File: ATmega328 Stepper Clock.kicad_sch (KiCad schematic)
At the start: 14 parts, among them IC1 ATMEGA328-AU, J2 SBH11-PBPC-D05-ST-BK, M1 Stepper_Motor_bipolar, M2 Stepper_Motor_bipolar, Q1 TCRT5000, Q2 TCRT5000, Y1 Crystal

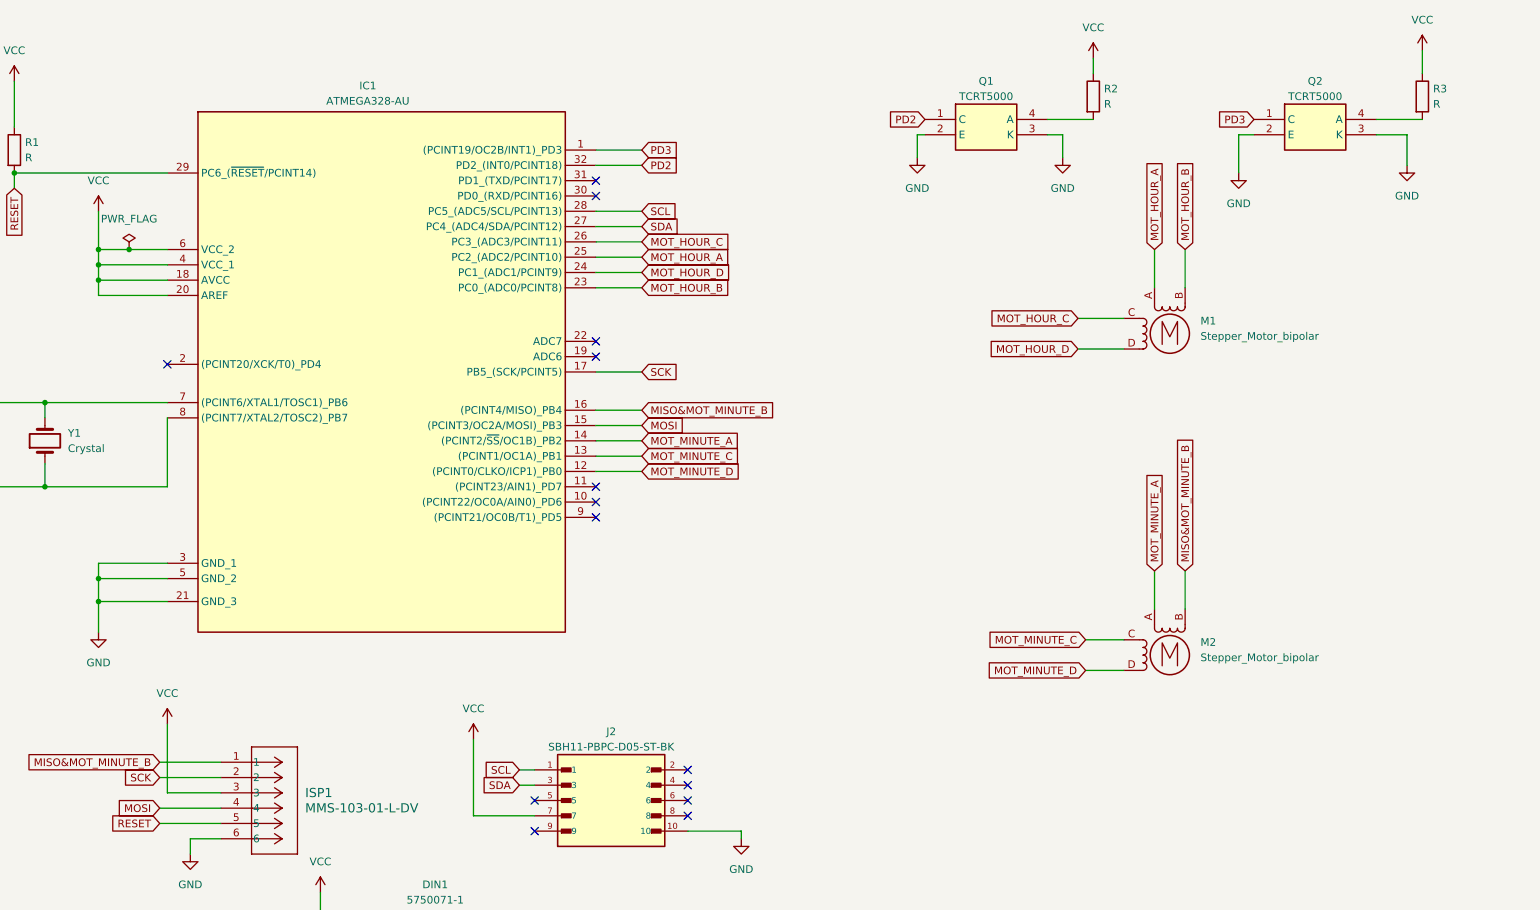
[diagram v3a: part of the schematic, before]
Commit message: I have made custom symbol for VID28-05 and assigned the footprint for it which sir gave me
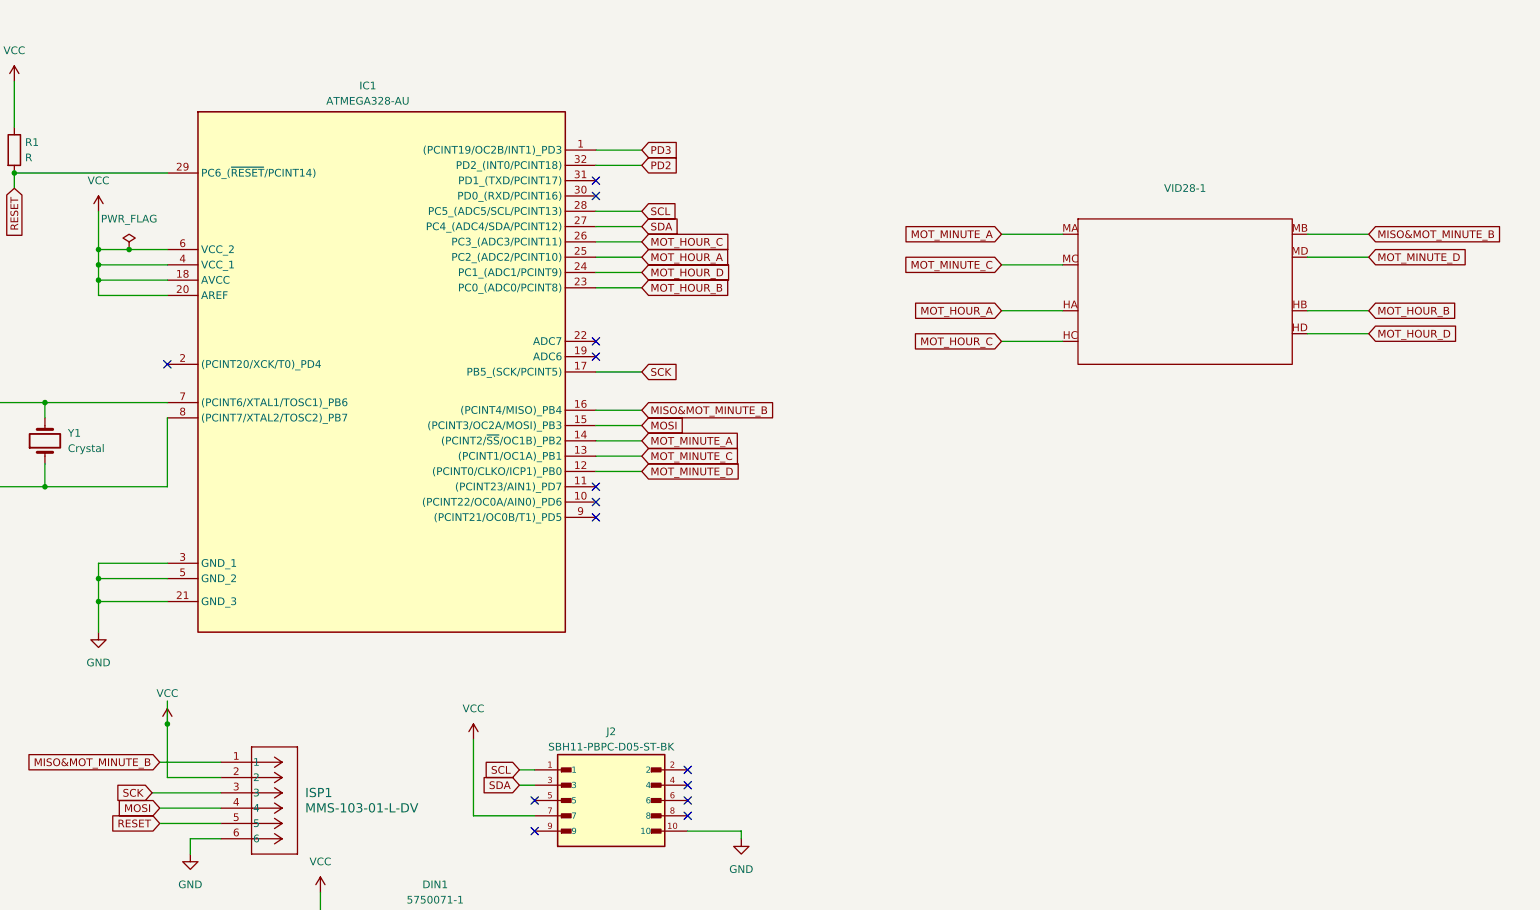
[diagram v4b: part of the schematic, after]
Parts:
- removed M1, M2: Stepper_Motor_bipolar, symbol Motor:Stepper_Motor_bipolar
- removed Q1, Q2: TCRT5000, SamacSys_Parts:TCRT5000, symbol SamacSys_Parts:TCRT5000
- removed R2, R3: R, Resistor_THT:R_Axial_DIN0414_L11.9mm_D4.5mm_P15.24mm_Horizontal, symbol Device:R
- added VID28-1: ~, VID28-05:VID28-05, symbol VID28-05:VID28-05
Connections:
- net MISO&MOT_MINUTE_B: now also VID28-1.MB
- net MOT_HOUR_A: now also VID28-1.HA
- net MOT_HOUR_B: now also VID28-1.HB
- net MOT_HOUR_C: now also VID28-1.HC
- net MOT_HOUR_D: now also VID28-1.HD
- net MOT_MINUTE_A: now also VID28-1.MA
- net MOT_MINUTE_C: now also VID28-1.MC
- net MOT_MINUTE_D: now also VID28-1.MD
- net SCK: now also ISP1.3; no longer ISP1.2
- net VCC: now also ISP1.2; no longer ISP1.3

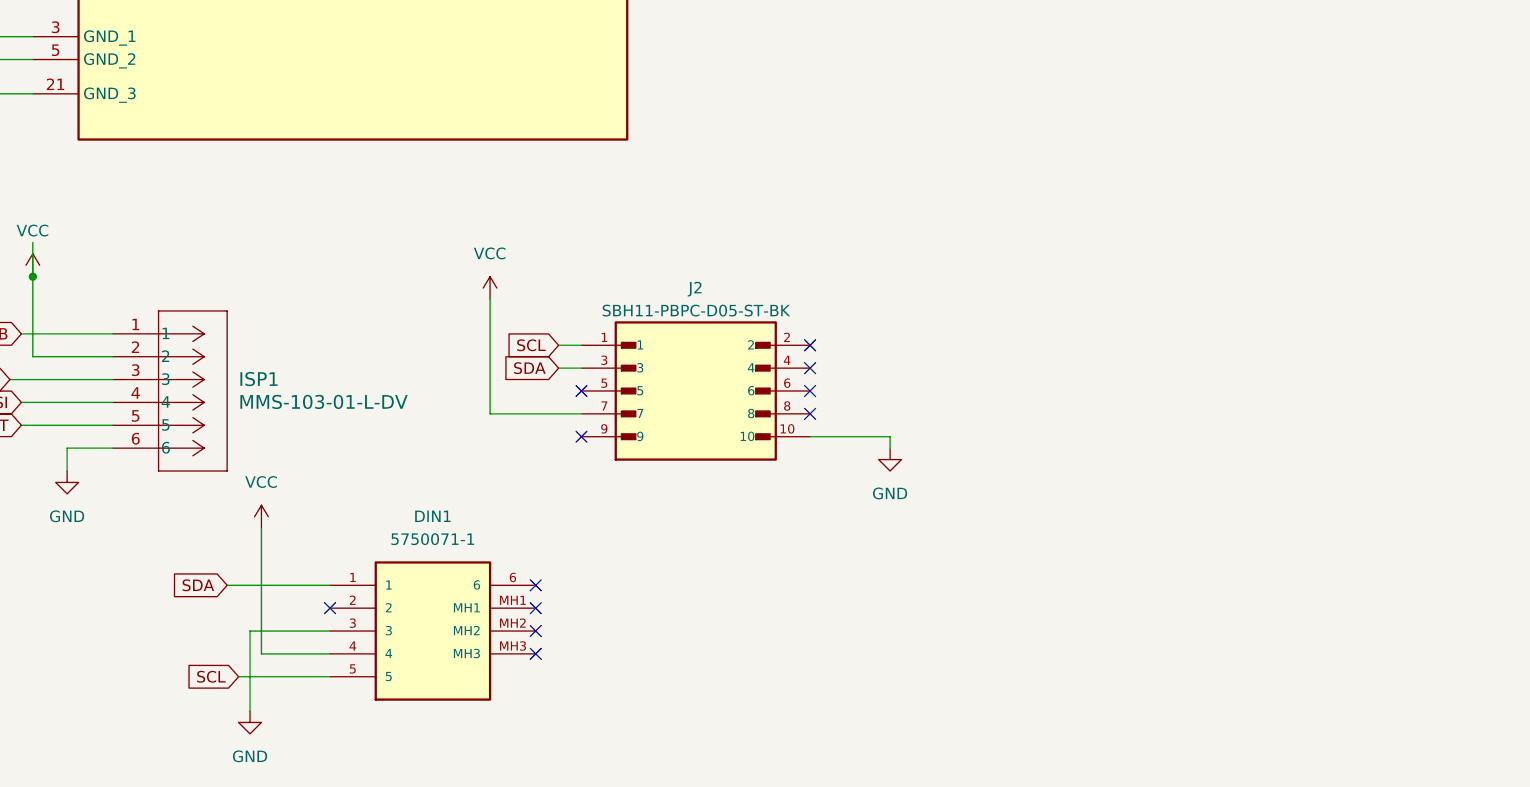
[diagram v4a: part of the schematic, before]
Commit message: Had to lot of changes like delete 10pin connectors,replace the DIN with 4-pin connector , hole size 3mm im starting the pcb layout all over again
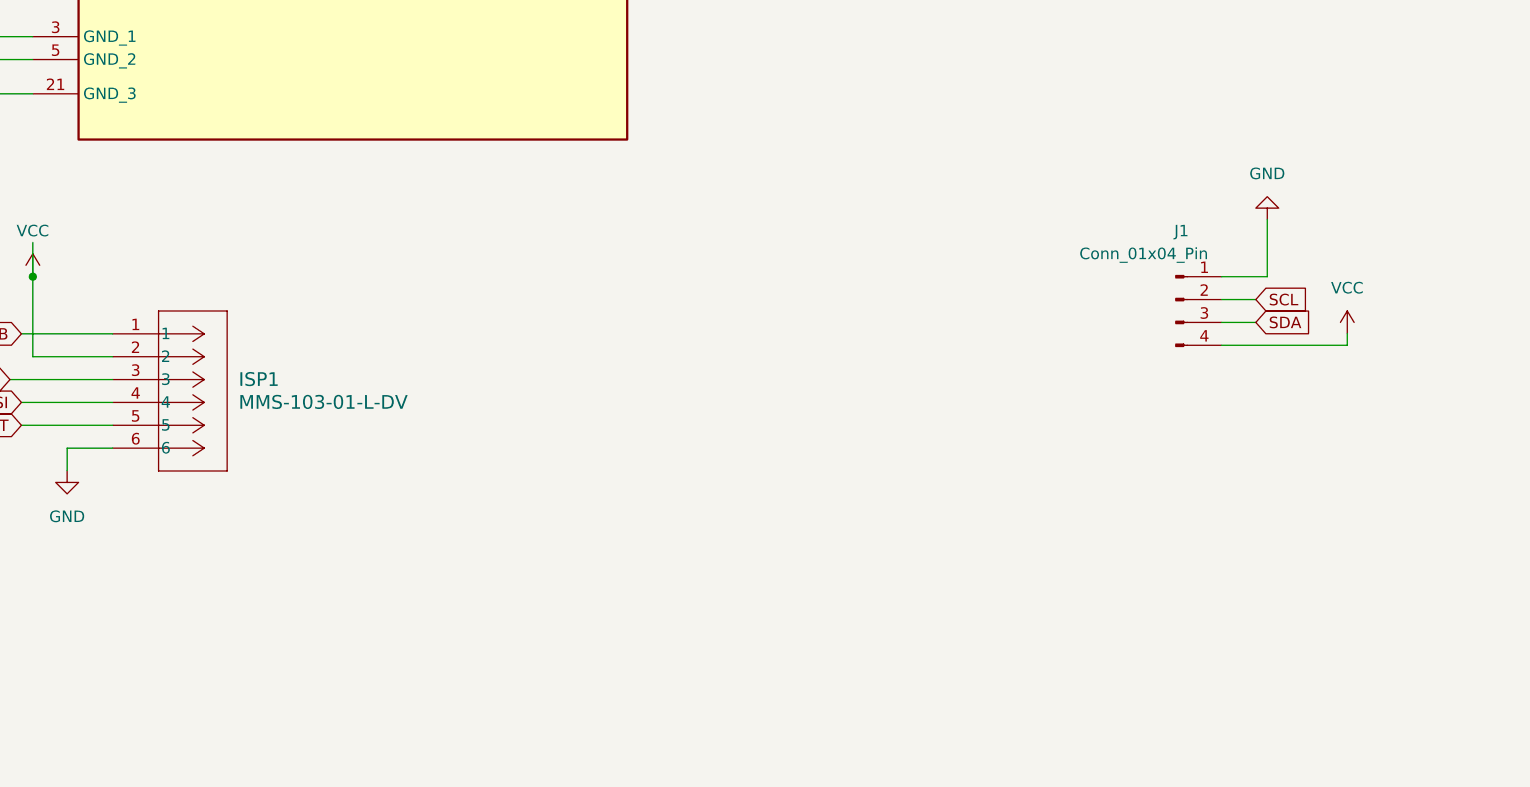
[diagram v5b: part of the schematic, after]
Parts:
- removed DIN1: 5750071-1, 5750071-1:57500711, symbol 5750071-1:5750071-1
- removed J2: SBH11-PBPC-D05-ST-BK, SBH11-PBPC-D05-ST-BK:SULLINS_SBH11-PBPC-D05-ST-BK, symbol SBH11-PBPC-D05-ST-BK:SBH11-PBPC-D05-ST-BK
- added J1: Conn_01x04_Pin, Connector_Wago:Wago_734-134_1x04_P3.50mm_Vertical, symbol Connector:Conn_01x04_Pin
- C1, C2: footprint Capacitor_THT:C_Axial_L5.1mm_D3.1mm_P15.00mm_Horizontal -> Capacitor_SMD:C_0805_2012Metric
- R1: footprint Resistor_THT:R_Axial_DIN0414_L11.9mm_D4.5mm_P15.24mm_Horizontal -> Resistor_SMD:R_1206_3216Metric
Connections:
- net GND: now also J1.1 (Pin_1)
- net SCL: now also J1.2 (Pin_2)
- net SDA: now also J1.3 (Pin_3)
- net VCC: now also J1.4 (Pin_4)
- no-connect marks 19 -> 8

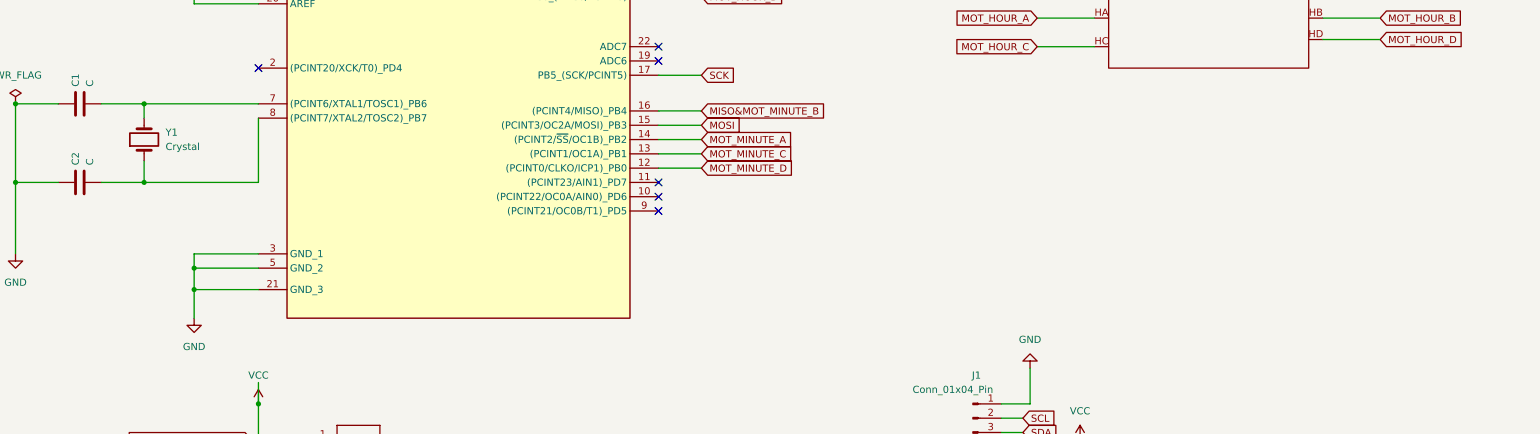
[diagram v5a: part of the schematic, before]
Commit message: changed the crystal to one which was available in the mouser website again made the PCB layout , all the SMD components are on the front and the THT are in the bottom
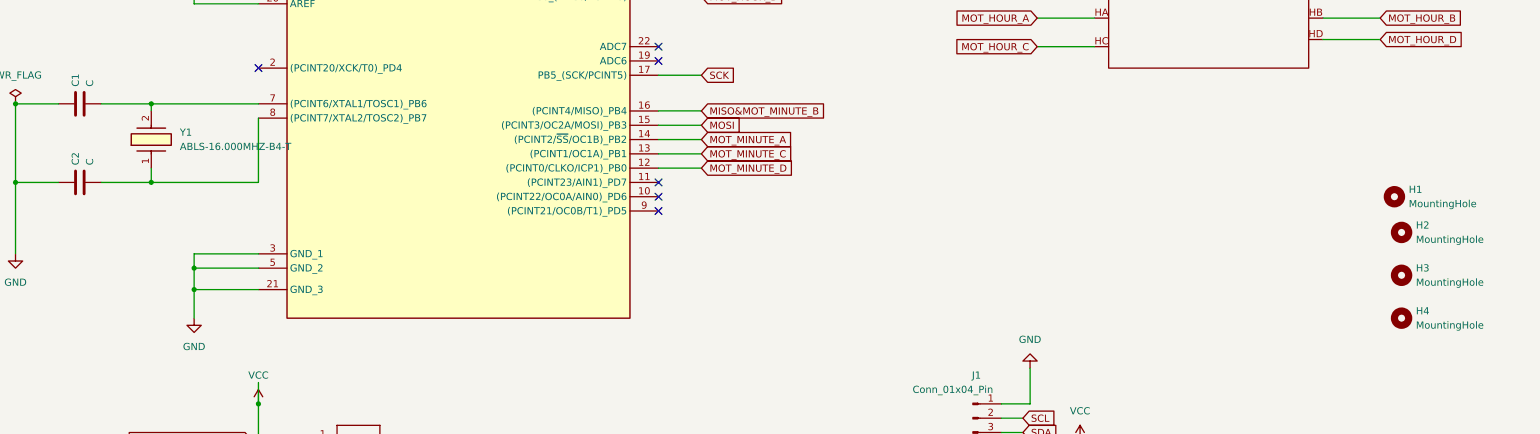
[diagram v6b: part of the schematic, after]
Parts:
- removed Y1: Crystal, Crystal:Crystal_AT310_D3.0mm_L10.0mm_Horizontal, symbol Device:Crystal
- added H1, H2, H3, H4: MountingHole, MountingHole:MountingHole_3mm, symbol Mechanical:MountingHole
- added Y1: ABLS-16.000MHZ-B4-T, SamacSys_Parts:ABLS, symbol SamacSys_Parts:ABLS-16.000MHZ-B4-T
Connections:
- net at C2.2, IC1.8 ((PCINT7/XTAL2/TOSC2)_PB7): now also Y1.1
- net at C1.2, IC1.7 ((PCINT6/XTAL1/TOSC1)_PB6): now also Y1.2
